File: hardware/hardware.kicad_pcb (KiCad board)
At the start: 2 copper layers, 42 x 42 mm, 40 parts, among them J1 Conn_01x06, J2 USB_C_Receptacle_USB2.0_14P, J3 Conn_01x04_Pin, Q1 BSS138, Q2 BSS138, U1 CH340C, U2 ESP32-WROOM-32, U3 AMS1117-3.3, U4 DRV8825PWPR

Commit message: finish pcb wiring
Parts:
- added J4: Conn_01x02_Pin, Connector_JST:JST_XH_B2B-XH-A_1x02_P2.50mm_Vertical, F.Cu at (84.0, 59.0)
- BOOT1, BTN1: footprint Button_Switch_SMD:SW_SPST_FSMSM -> Button_Switch_SMD:SW_Push_SPST_NO_Alps_SKRK
- EN1: footprint Button_Switch_SMD:SW_Push_1P1T-MP_NO_Horizontal_Alps_SKRTLAE010 -> Button_Switch_SMD:SW_Push_SPST_NO_Alps_SKRK
- J3: footprint TerminalBlock_Phoenix:TerminalBlock_Phoenix_MPT-0,5-4-2.54_1x04_P2.54mm_Horizontal -> Connector_JST:JST_XH_B4B-XH-A_1x04_P2.50mm_Vertical
- moved J1 158.7 mm to (82.0, 34.4)
- moved C9 156.7 mm to (90.5, 59.0), turned to 90 degrees
- moved BTN1 154.8 mm to (95.0, 33.0)
- moved BOOT1 152.3 mm to (95.0, 38.0)
- moved D1 148.9 mm to (116.0, 31.5)
- moved D2 140.6 mm to (116.7, 51.5)
- moved TP1 127.7 mm to (81.5, 53.0), turned to -90 degrees
- moved R8 118.1 mm to (94.0, 46.7), turned to 90 degrees
- moved R7 111.1 mm to (92.0, 67.0), turned to 180 degrees
- moved C5 109.3 mm to (97.5, 46.7), turned to 90 degrees
- moved R5 108.8 mm to (92.0, 71.0), turned to 180 degrees
- moved C6 106.9 mm to (92.0, 65.0), turned to 180 degrees
- moved C7 105.4 mm to (92.0, 69.0)
- moved R2 105.0 mm to (103.5, 49.2), turned to 90 degrees
- moved R4 103.8 mm to (120.5, 34.0), turned to 90 degrees
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- renumbered TP4 to FAULT, TP3 to REF
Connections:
- C7 pad 1: +BATT -> +5V
- C9 pad 1: +BATT -> +5V
- JP1 pad 3: VBUS -> +3.3V
- JP2 pad 3: VBUS -> +3.3V
- JP3 pad 3: VBUS -> +3.3V
- R7 pad 2: +BATT -> +5V
- R9 pad 2: VBUS -> +3.3V
- U2 pad 26: unconnected-(U2-IO4-Pad26) -> STEP
- U2 pad 29: unconnected-(U2-IO5-Pad29) -> DIR
- U4 pad 10: Net-(J3-Pin_2) -> Net-(J3-Pin_3)
- U4 pad 11: +BATT -> +5V
- U4 pad 4: +BATT -> +5V
- U4 pad 5: Net-(J3-Pin_3) -> Net-(J3-Pin_2)
- U4 pad 7: Net-(J3-Pin_4) -> Net-(J3-Pin_1)
- U4 pad 8: Net-(J3-Pin_1) -> Net-(J3-Pin_4)
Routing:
- net +5V: track 0.00 -> 100.2 mm, vias 0 -> 5
- net +3V3: track 0.00 -> 54.4 mm, vias 0 -> 1
- net DIR: track 0.00 -> 34.7 mm, vias 0 -> 3
- net STEP: track 0.00 -> 32.3 mm, vias 0 -> 2
- net ESP32_EN: track 0.00 -> 32.1 mm, vias 0 -> 2
- net Net-(U2-IO13): track 0.00 -> 29.6 mm, vias 0 -> 1
- net Net-(Q1-G): track 0.00 -> 28.2 mm, vias 0 -> 3
- net RX-PROG: track 0.00 -> 27.6 mm, vias 0 -> 1
- net +3.3V: track 0.00 -> 26.4 mm
- net TX-PROG: track 0.00 -> 26.2 mm, vias 0 -> 1
- net ESP32_IO0: track 0.00 -> 25.9 mm, vias 0 -> 1
- net Net-(U4-NFAULT): track 0.00 -> 20.7 mm, vias 0 -> 2
- net Net-(Q1-S): track 0.00 -> 20.5 mm, vias 0 -> 2
- net Net-(U4-AVREF): track 0.00 -> 18.0 mm
- net BTN1: track 0.00 -> 16.4 mm, vias 0 -> 1
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- added copper zone on B.Cu, net GND
- added copper zone on F.Cu, net GND

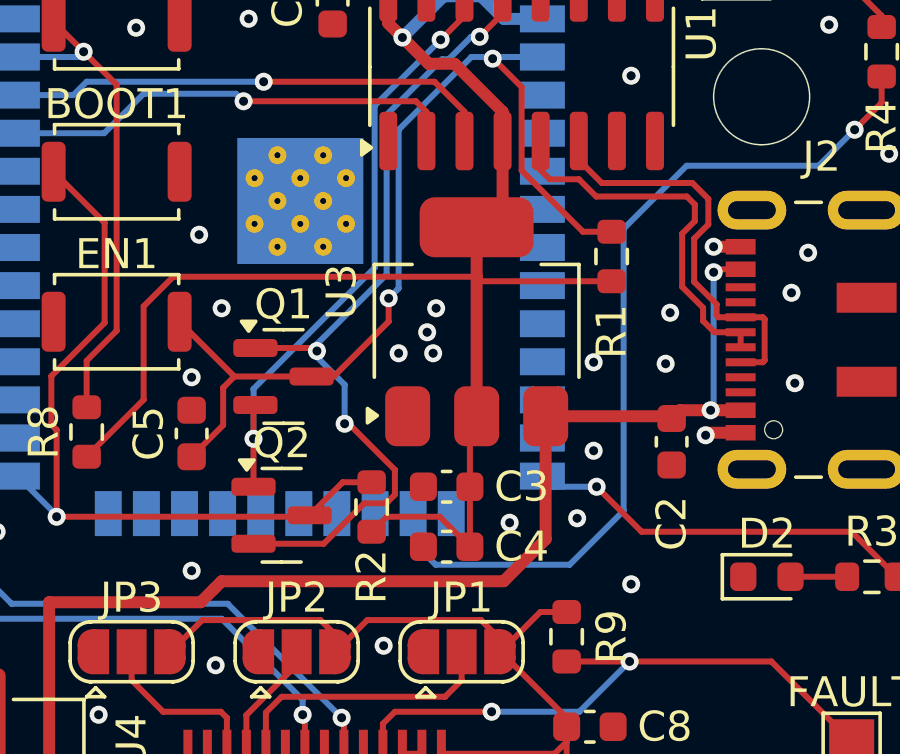
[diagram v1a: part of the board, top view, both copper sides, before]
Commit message: gnd capacitor pcb wiring
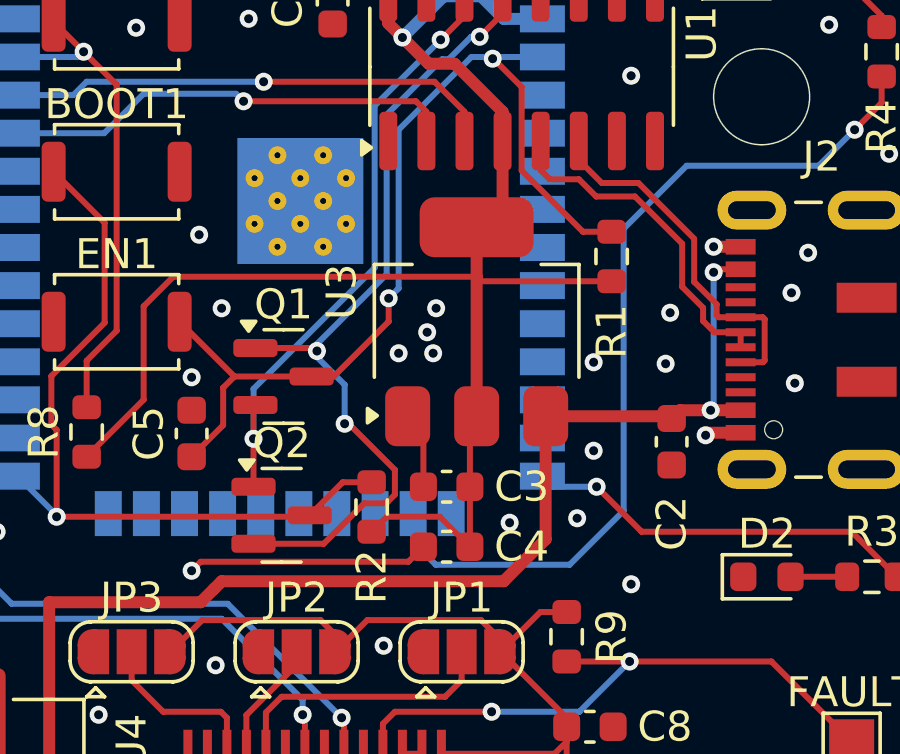
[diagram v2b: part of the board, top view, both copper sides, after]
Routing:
- net GND: track 2.10 -> 12.7 mm
- net D-: track 13.7 -> 12.3 mm
- net D+: track 12.8 -> 11.5 mm
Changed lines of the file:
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@@
+	)
+	(segment
+		(start 97.8 51)
+		(end 97.5 51.3)
+		(width 0.2)
+		(layer "F.Cu")
+		(net 2)
 	)
 	(segment
@@
 	)
 	(segment
+		(start 105.225 50.5)
+		(end 104.725 51)
+		(width 0.2)
+		(layer "F.Cu")
+		(net 2)
+	)
+	(segment
+		(start 105.225 46.675)
+		(end 104.7 46.15)
+		(width 0.2)
+		(layer "F.Cu")
+		(net 2)
+	)
+	(segment
+		(start 104.725 51)
+		(end 97.8 51)
+		(width 0.2)
+		(layer "F.Cu")
+		(net 2)
+	)
+	(segment
 		(start 115.8 46.7)
 		(end 114.716797 46.7)
@@
 		(end 114.9 40.499997)
 		(width 0.4)
+		(layer "F.Cu")
+		(net 2)
+	)
+	(segment
+		(start 105.225 48.5)
+		(end 105.225 46.675)
+		(width 0.2)
 		(layer "F.Cu")
 		(net 2)
@@
 	)
 	(segment
+		(start 114.999 42.786)
+		(end 114.999 42.418239)
+		(width 0.2)
+		(layer "F.Cu")
+		(net 17)
+	)
+	(segment
+		(start 112.394242 38.375)
+		(end 111.171397 38.375)
+		(width 0.2)
+		(layer "F.Cu")
+		(net 17)
+	)
+	(segment
+		(start 115.8 44.35)
+		(end 116.537 44.35)
+		(width 0.2)
+		(layer "F.Cu")
+		(net 17)
+	)
+	(segment
+		(start 114.999 42.418239)
+		(end 114.25 41.669239)
+		(width 0.2)
+		(layer "F.Cu")
+		(net 17)
+	)
+	(segment
+		(start 116.601 44.286)
+		(end 116.601 42.914)
+		(width 0.2)
+		(layer "F.Cu")
+		(net 17)
+	)
+	(segment
+		(start 114.25 41.669239)
+		(end 114.25 40.230758)
+		(width 0.2)
+		(layer "F.Cu")
+		(net 17)
+	)
+	(segment
+		(start 115.8 42.85)
+		(end 115.063 42.85)
+		(width 0.2)
+		(layer "F.Cu")
+		(net 17)
+	)
+	(segment
+		(start 114.25 40.230758)
+		(end 112.394242 38.375)
+		(width 0.2)
+		(layer "F.Cu")
+		(net 17)
+	)
+	(segment
+		(start 116.537 44.35)
+		(end 116.601 44.286)
+		(width 0.2)
+		(layer "F.Cu")
+		(net 17)
+	)
+	(segment
+		(start 116.537 42.85)
+		(end 115.8 42.85)
+		(width 0.2)
+		(layer "F.Cu")
+		(net 17)
+	)
+	(segment
+		(start 110.405 37.608603)
+		(end 110.405 36.975)
+		(width 0.2)
+		(layer "F.Cu")
+		(net 17)
+	)
+	(segment
 		(start 111.171397 38.375)
 		(end 110.405 37.608603)
@@
 	)
 	(segment
-		(start 114.25 41.669239)
-		(end 114.25 40.230758)
-		(width 0.2)
-		(layer "F.Cu")
-		(net 17)
-	)
-	(segment
-		(start 115.8 44.35)
-		(end 116.537 44.35)
-		(width 0.2)
-		(layer "F.Cu")
-		(net 17)
-	)
-	(segment
 		(start 115.063 42.85)
 		(end 114.999 42.786)
@@
 	)
 	(segment
-		(start 116.601 44.286)
-		(end 116.601 42.914)
-		(width 0.2)
-		(layer "F.Cu")
-		(net 17)
-	)
-	(segment
-		(start 110.405 37.608603)
-		(end 110.405 36.975)
-		(width 0.2)
-		(layer "F.Cu")
-		(net 17)
-	)
-	(segment
-		(start 116.537 44.35)
-		(end 116.601 44.286)
-		(width 0.2)
-		(layer "F.Cu")
-		(net 17)
-	)
-	(segment
-		(start 114.25 40.230758)
-		(end 114.724 39.756758)
-		(width 0.2)
-		(layer "F.Cu")
-		(net 17)
-	)
-	(segment
-		(start 115.8 42.85)
-		(end 115.063 42.85)
-		(width 0.2)
-		(layer "F.Cu")
-		(net 17)
-	)
-	(segment
-		(start 114.999 42.786)
-		(end 114.999 42.418239)
-		(width 0.2)
-		(layer "F.Cu")
-		(net 17)
-	)
-	(segment
-		(start 116.537 42.85)
-		(end 115.8 42.85)
-		(width 0.2)
-		(layer "F.Cu")
-		(net 17)
-	)
-	(segment
-		(start 114.193198 38.375)
-		(end 111.171397 38.375)
-		(width 0.2)
-		(layer "F.Cu")
-		(net 17)
-	)
-	(segment
-		(start 114.999 42.418239)
-		(end 114.25 41.669239)
-		(width 0.2)
-		(layer "F.Cu")
-		(net 17)
-	)
-	(segment
 		(start 116.601 42.914)
 		(end 116.537 42.85)
@@
 	)
 	(segment
-		(start 114.724 38.905802)
-		(end 114.193198 38.375)
-		(width 0.2)
-		(layer "F.Cu")
-		(net 17)
-	)
-	(segment
-		(start 114.724 39.756758)
-		(end 114.724 38.905802)
-		(width 0.2)
-		(layer "F.Cu")
-		(net 17)
+		(start 115.8 43.85)
+		(end 115.8 43.35)
+		(width 0.2)
+		(layer "F.Cu")
+		(net 20)
 	)
 	(segment
@@
 	)
 	(segment
-		(start 115.8 43.85)
-		(end 115.8 43.35)
-		(width 0.2)
-		(layer "F.Cu")
-		(net 20)
-	)
-	(segment
 		(start 114.926632 43.35)
 		(end 114.54902 42.972388)
@@
 	)
 	(segment
-		(start 113.85 41.834924)
-		(end 113.85 40.065072)
+		(start 112.278556 38.825)
+		(end 110.985 38.825)
 		(width 0.2)
 		(layer "F.Cu")
@@
 	)
 	(segment
-		(start 113.85 40.065072)
-		(end 114.27402 39.641052)
+		(start 113.85 40.396444)
+		(end 112.278556 38.825)
+		(width 0.2)
+		(layer "F.Cu")
+		(net 20)
+	)
+	(segment
+		(start 110.985 38.825)
+		(end 110.411 38.251)
 		(width 0.2)
 		(layer "F.Cu")
@@
 	)
 	(segment
-		(start 110.985 38.825)
-		(end 110.411 38.251)
+		(start 109.135 37.949999)
+		(end 109.135 36.975)
 		(width 0.2)
 		(layer "F.Cu")
@@
 	)
 	(segment
-		(start 114.006802 38.825)
-		(end 110.985 38.825)
-		(width 0.2)
-		(layer "F.Cu")
-		(net 20)
-	)
-	(segment
-		(start 109.135 37.949999)
-		(end 109.135 36.975)
+		(start 113.85 41.834924)
+		(end 113.85 40.396444)
 		(width 0.2)
 		(layer "F.Cu")
@@
 		(width 0.2)
 		(layer "F.Cu")
-		(net 20)
-	)
-	(segment
-		(start 114.27402 39.092218)
-		(end 114.006802 38.825)
-		(width 0.2)
-		(layer "F.Cu")
-		(net 20)
-	)
-	(segment
-		(start 114.27402 39.641052)
-		(end 114.27402 39.092218)
-		(width 0.2)
-		(layer "F.Cu")
